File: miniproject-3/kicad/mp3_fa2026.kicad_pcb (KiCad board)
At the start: 2 copper layers, 38.1 x 54.6 mm, 41 parts, among them J1 USB4105-GF-A, J2 LEFT, J3 RIGHT, J4 DEBUG, U1 RP2354A, U2 MCP1702T-3302E_CB, X1 IQXO-791_12MHz

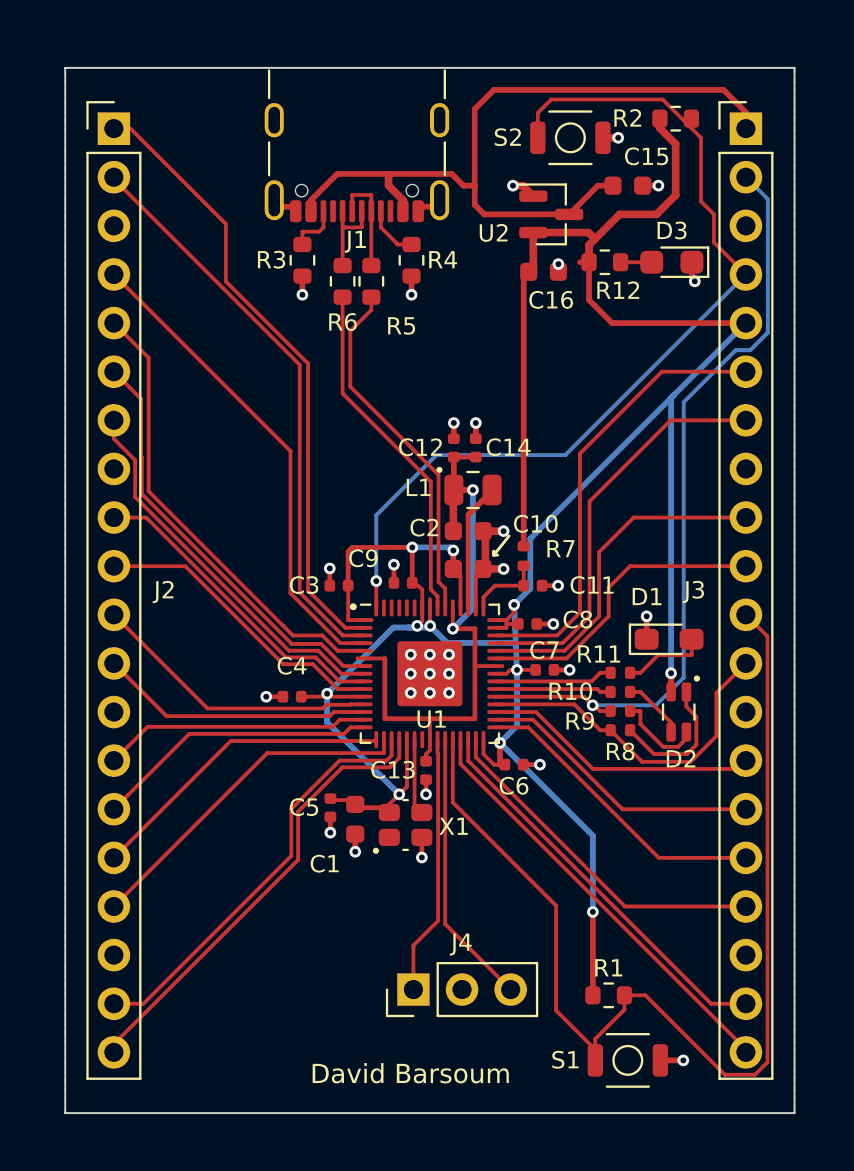
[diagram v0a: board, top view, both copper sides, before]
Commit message: bypass caps closer and routing
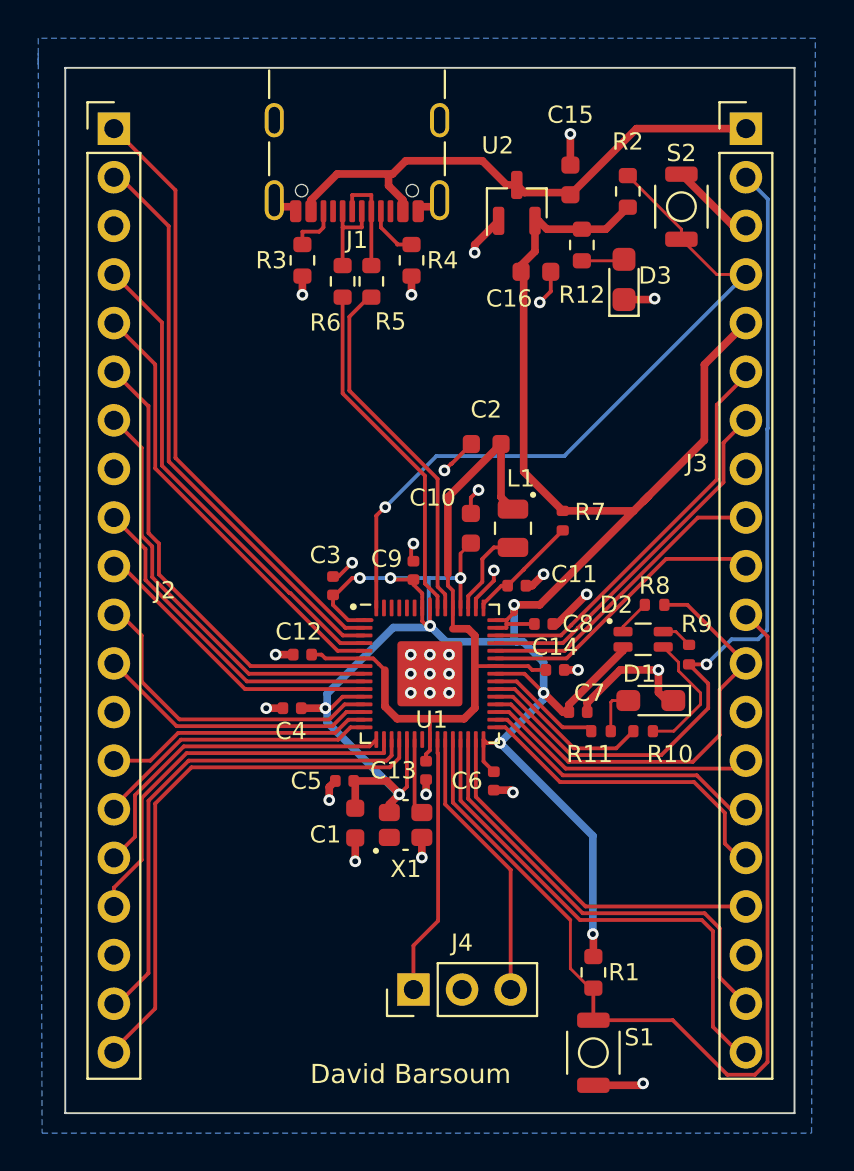
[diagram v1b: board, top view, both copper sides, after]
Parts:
- moved C12 13.4 mm to (194.0, 124.0), turned to 0 degrees
- moved C14 12.3 mm to (207.2, 124.8), turned to 180 degrees
- moved S2 6.83 mm to (213.8, 100.6), turned to 90 degrees
- moved R8 6.79 mm to (212.4, 121.4), turned to 180 degrees
- moved R9 4.65 mm to (214.2, 124.0), turned to 90 degrees
- moved C2 4.65 mm to (203.6, 113.0), turned to 0 degrees
- moved R2 4.55 mm to (211.0, 99.8), turned to 90 degrees
- moved D2 4.23 mm to (211.8, 123.2), turned to 90 degrees
- moved D1 3.34 mm to (212.2, 126.4), turned to 180 degrees
- moved R11 3.21 mm to (209.6, 128.0)
- moved C15 3.01 mm to (208.0, 99.2), turned to -90 degrees
- moved L1 2.89 mm to (205.0, 117.4), turned to -90 degrees
- moved C7 2.80 mm to (208.4, 127.0)
- moved R7 2.75 mm to (207.6, 117.0)
- moved D3 2.66 mm to (210.8, 104.4), turned to 90 degrees
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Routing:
- net +3V3: track 158.4 -> 138.0 mm, vias 11 -> 10
- net GND: track 27.4 -> 44.2 mm, vias 33 -> 32
- net +5V: track 41.1 -> 28.5 mm
- net /BOOT: track 48.4 -> 37.8 mm
- net /GPIO22: track 17.8 -> 23.4 mm
- net Net-(D2-Pad1): track 7.16 -> 1.87 mm
- net /GPIO15: track 24.0 -> 28.6 mm
- net /GPIO23: track 40.6 -> 45.1 mm
- net /RUN: track 56.6 -> 52.2 mm
- net /GPIO16: track 22.5 -> 26.5 mm
- net /GPIO14: track 22.2 -> 26.0 mm
- net +1V1: track 33.3 -> 37.0 mm, vias 2 -> 0
- net Net-(D2-Pad4): track 3.30 -> 6.88 mm
- net Net-(D2-Pad2): track 4.63 -> 1.64 mm
- net /GPIO24: track 6.06 -> 8.85 mm
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
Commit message: add v2 name
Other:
- board text added: "David Barsoum v2"
- board text removed: "David Barsoum"
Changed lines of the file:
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@@
 		(layer "Edge.Cuts")
 	)
-	(gr_text "David Barsoum"
-		(at 194.4 146.504835 0)
+	(gr_text "David Barsoum v2"
+		(at 192 146 0)
 		(layer "F.SilkS")
 		(effects
